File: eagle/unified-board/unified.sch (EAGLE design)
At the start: 96 parts, among them IC101 THAT151x, J1 eqout, J101 phantom, J103 eqout, J601 out2, U101 lme49710, U601 LM3915N, U602 lme49710

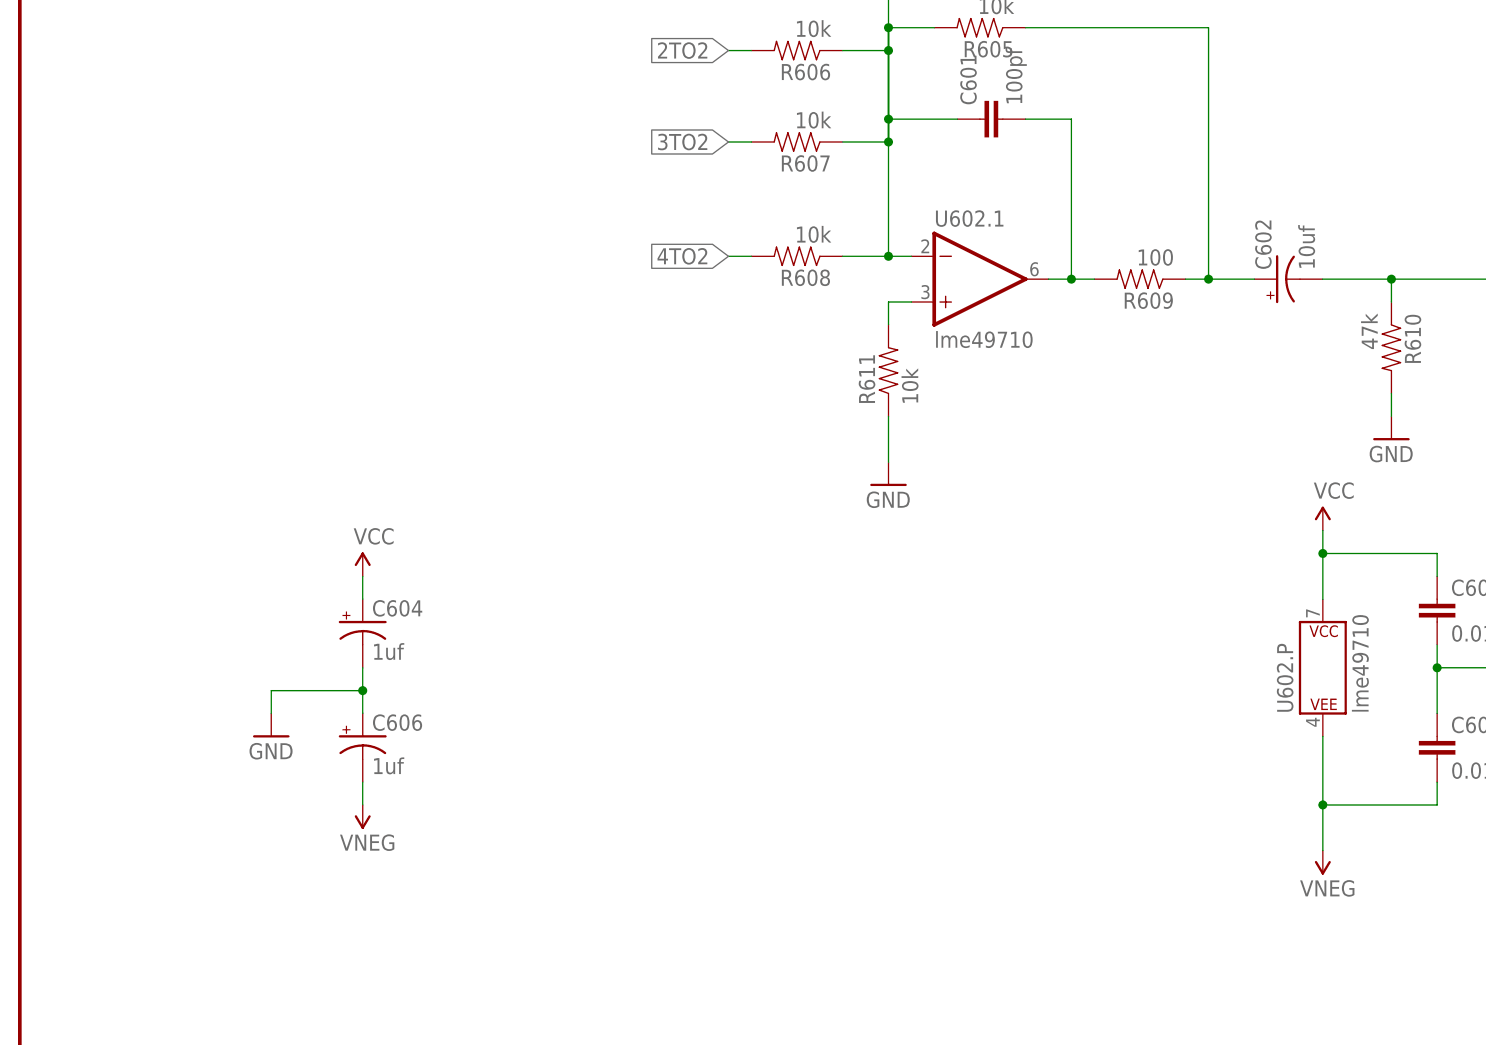
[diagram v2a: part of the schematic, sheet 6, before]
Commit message: Capacitor update
sourced & created a bunch of caps.
pushed components around more & better.
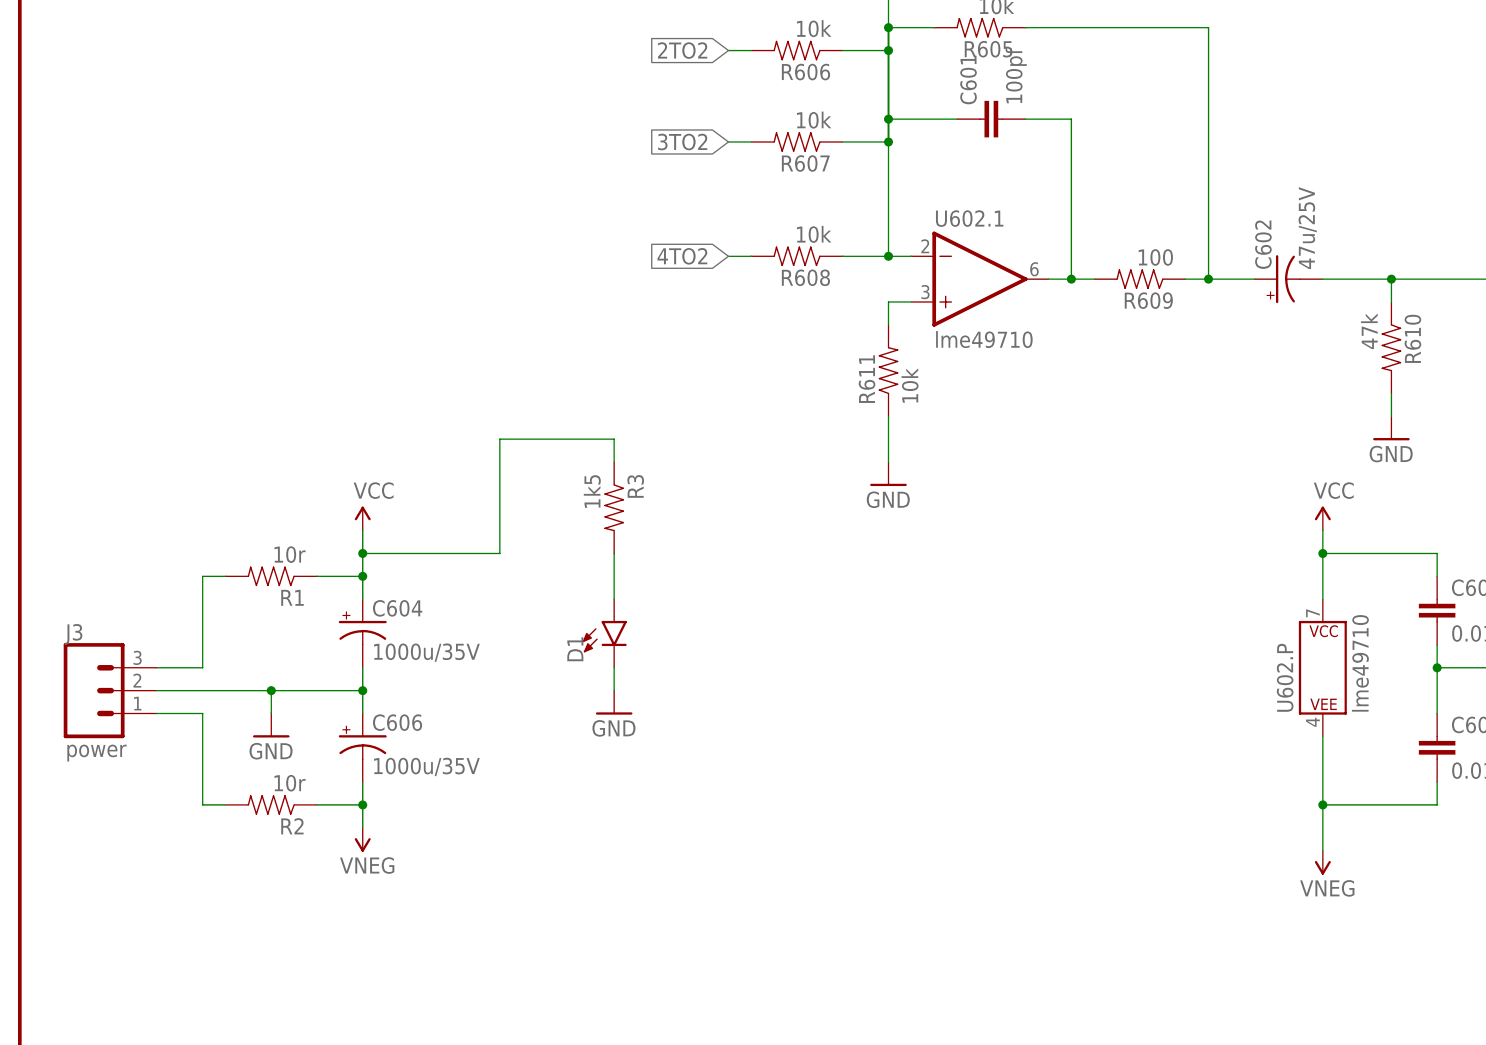
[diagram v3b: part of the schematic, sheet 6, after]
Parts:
- added D1: (no value), SparkFun-LED:LED5MM
- added J3: power, SparkFun-Connectors:CONN_03POLAR_LOCK
- added R1, R2: 10r, SparkFun-Resistors:RESISTORAXIAL-0.3
- added R3: 1k5, SparkFun-Resistors:RESISTORAXIAL-0.3
- C105, C114: value 22u -> 47u/63V; device SparkFun-Capacitors:100UF-25V-20%(PTH) -> mixer:CAP-LYTIC47U/63V
- C106, C107, C112, C116, C119, C121: value 470p -> 470pf; device SparkFun-Capacitors:CAPPTH -> mixer:CAP-CERAMIC470PF
- C108, C120: value 47p -> 47pf; device SparkFun-Capacitors:CAPPTH -> mixer:CAP-CERAMIC47PF
- C109, C117, C118, C122: value 22u -> 47u/25V; device SparkFun-Capacitors:100UF-25V-20%(PTH) -> mixer:CAP-LYTIC47U/25V
- C110, C601: device SparkFun-Capacitors:CAPPTH -> mixer:CAP-CERAMIC100PF
- C115: value 22u -> 6800u/25V; device SparkFun-Capacitors:100UF-25V-20%(PTH) -> mixer:CAP-LYTIC6800U/10V
- C602: value 10uf -> 47u/25V; device SparkFun-Capacitors:10UF-25V-20%(PTH) -> mixer:CAP-LYTIC47U/25V
- C604, C606: value 1uf -> 1000u/35V; device SparkFun-Capacitors:CAP_POLPTH2 -> mixer:CAP-LYTIC1000U/35V
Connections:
- new net N$18: J3.3, R1.2
- new net N$5: J3.1, R2.2
- new net N$54: D1.A, R3.2
- net GND: now also D1.C, J3.2, VR104.A, VR105.A
- net VCC: now also R1.1, R3.1
- net VNEG: now also R2.1
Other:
- note added: "Check DC offset at various EQ settings, possibly can omit C118"
- note added: "Check DC offset at various gains, possibly can omit C109"

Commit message: Conforming parts on BOM for ordering.
verified mouser & SFe part #s.
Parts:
- C603: device SparkFun-Capacitors:CAPPTH -> mixer:CAP-CERAMIC100PF
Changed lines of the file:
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@@
 <setting verticaltext="up"/>
 </settings>
-<grid distance="0.1" unitdist="inch" unit="inch" style="lines" multiple="1" display="yes" altdistance="0.01" altunitdist="inch" altunit="inch"/>
+<grid distance="0.1" unitdist="inch" unit="inch" style="lines" multiple="1" display="no" altdistance="0.01" altunitdist="inch" altunit="inch"/>
 <layers>
 <layer number="1" name="Top" color="4" fill="1" visible="no" active="no"/>
@@
 <part name="SUPPLY606" library="SparkFun-Aesthetics" deviceset="VCC" device=""/>
 <part name="FB601" library="mixer" deviceset="FB" device="" value="FB"/>
-<part name="C603" library="SparkFun-Capacitors" deviceset="CAP" device="PTH" value="100pf"/>
+<part name="C603" library="mixer" deviceset="CAP-CERAMIC" device="100PF" value="100pf"/>
 <part name="GND605" library="SparkFun-Aesthetics" deviceset="GND" device=""/>
 <part name="D602" library="mixer" deviceset="RECTIFIER" device="RB15X"/>

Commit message: Duplicated input channels.
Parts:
- removed D1: (no value), SparkFun-LED:LED5MM
- removed J1: eqout, SparkFun-Connectors:M01NOSILK-KIT
- removed J3: power, SparkFun-Connectors:CONN_03POLAR_LOCK
- removed R1, R2: 10r, SparkFun-Resistors:RESISTORAXIAL-0.3
- removed R3: 1k5, SparkFun-Resistors:RESISTORAXIAL-0.3
- added C201, C202, C301, C302, C401, C402: 47pf, mixer:CAP-CERAMIC47PF
- added C203, C204, C205, C206, C212, C213, C303, C304, C305, C306, C312, C313, C403, C404, C405, C406, C412, C413: 470pf, mixer:CAP-CERAMIC470PF
- added C207, C208, C307, C308, C407, C408: 47u/63V, mixer:CAP-LYTIC47U/63V
- added C209, C210, C214, C220, C309, C310, C314, C320, C409, C410, C414, C420: 47u/25V, mixer:CAP-LYTIC47U/25V
- added C211, C311, C411: 6800u/25V, mixer:CAP-LYTIC6800U/10V
- added C215, C216, C315, C316, C415, C416: 0.1uf, mixer:WIMA-MKS20.1UF
- added C217, C218, C317, C318, C417, C418: 0.015uf, mixer:WIMA-MKS20.015UF
- added C219, C319, C419: 100pf, mixer:CAP-CERAMIC100PF
- added C221, C222, C321, C322, C421, C422: 0.01uf, mixer:WIMA-MKS20.01UF
- added D201, D301, D401: RECTIFIERRB15X, mixer:RECTIFIERRB15X
- added D202, D203, D302, D303, D402, D403: 1N4148, SparkFun-DiscreteSemi:DIODE1N4148
- added D603: RED, SparkFun-LED:LED_BARGRAPH_10RED
- added IC201, IC301, IC401: THAT151x, mosfet:THAT151X
- added J105, J204, J205, J304, J305, J404, J405: eqout, SparkFun-Connectors:M01NOSILK-KIT
- added J201, J202, J301, J302, J401, J402: (no value), SparkFun-Connectors:M031X03_NO_SILK
- added J203, J303, J403: phantom, SparkFun-Connectors:M01NOSILK-KIT
- added J206, J306, J406: (no value), SparkFun-Connectors:CONN_05PTH_LONGPADS
- added J602: out2, SparkFun-Connectors:CONN_02LOCK_LONGPADS
- added R201, R202, R301, R302, R401, R402: 6k8, SparkFun-Resistors:10KOHM-1/4W-1%(PTH)HORIZ
- added R203, R204, R303, R304, R403, R404: 10, SparkFun-Resistors:10KOHM-1/4W-1%(PTH)HORIZ
- added R205, R206, R305, R306, R405, R406: 4k99, SparkFun-Resistors:10KOHM-1/4W-1%(PTH)HORIZ
- added R207, R307, R407: 22k, SparkFun-Resistors:10KOHM-1/4W-1%(PTH)HORIZ
- added R208, R209, R308, R309, R408, R409: 1k2, SparkFun-Resistors:10KOHM-1/4W-1%(PTH)HORIZ
- added R210, R310, R410: 5, SparkFun-Resistors:10KOHM-1/4W-1%(PTH)HORIZ
- added R211, R212, R311, R312, R411, R412: 1k8, SparkFun-Resistors:10KOHM-1/4W-1%(PTH)HORIZ
- added R213, R313, R413: 12k, SparkFun-Resistors:10KOHM-1/4W-1%(PTH)HORIZ
- added R214, R215, R216, R314, R315, R316, R414, R415, R416: 1k, SparkFun-Resistors:10KOHM-1/4W-1%(PTH)HORIZ
- added R612, R613, R614: ???, SparkFun-Resistors:RESISTORAXIAL-0.3
- added U201, U301, U401: lme49710, mixer:OPAMPLME49710
- added VR201, VR301, VR401: 10K, mixer:POTROT-SW-POT
- added VR202, VR203, VR204, VR205, VR302, VR303, VR304, VR305, VR402, VR403, VR404, VR405: 10K, mixer:POT10K-VERTPIN
- C101, C102: value 0.01uf -> 47pf; device mixer:WIMA-MKS20.01UF -> mixer:CAP-CERAMIC47PF
- C103: value 0.015uf -> 470pf; device mixer:WIMA-MKS20.015UF -> mixer:CAP-CERAMIC470PF
- C104, C113: value 0.1uf -> 470pf; device mixer:WIMA-MKS20.1UF -> mixer:CAP-CERAMIC470PF
- C105: value 47u/63V -> 470pf; device mixer:CAP-LYTIC47U/63V -> mixer:CAP-CERAMIC470PF
- C107: value 470pf -> 47u/63V; device mixer:CAP-CERAMIC470PF -> mixer:CAP-LYTIC47U/63V
- C108: value 47pf -> 47u/63V; device mixer:CAP-CERAMIC47PF -> mixer:CAP-LYTIC47U/63V
- C110: value 100pf -> 47u/25V; device mixer:CAP-CERAMIC100PF -> mixer:CAP-LYTIC47U/25V
- C111: value 0.015uf -> 6800u/25V; device mixer:WIMA-MKS20.015UF -> mixer:CAP-LYTIC6800U/10V
- C114: value 47u/63V -> 47u/25V; device mixer:CAP-LYTIC47U/63V -> mixer:CAP-LYTIC47U/25V
- C115: value 6800u/25V -> 0.1uf; device mixer:CAP-LYTIC6800U/10V -> mixer:WIMA-MKS20.1UF
- C116: value 470pf -> 0.1uf; device mixer:CAP-CERAMIC470PF -> mixer:WIMA-MKS20.1UF
- C117, C118: value 47u/25V -> 0.015uf; device mixer:CAP-LYTIC47U/25V -> mixer:WIMA-MKS20.015UF
- C119: value 470pf -> 100pf; device mixer:CAP-CERAMIC470PF -> mixer:CAP-CERAMIC100PF
- C120: value 47pf -> 47u/25V; device mixer:CAP-CERAMIC47PF -> mixer:CAP-LYTIC47U/25V
- C121: value 470pf -> 0.01uf; device mixer:CAP-CERAMIC470PF -> mixer:WIMA-MKS20.01UF
- C122: value 47u/25V -> 0.01uf; device mixer:CAP-LYTIC47U/25V -> mixer:WIMA-MKS20.01UF
- C601: value 100pf -> 1000u/35V; device mixer:CAP-CERAMIC100PF -> mixer:CAP-LYTIC1000U/35V
- C602: value 47u/25V -> 1000u/35V; device mixer:CAP-LYTIC47U/25V -> mixer:CAP-LYTIC1000U/35V
- C604: value 1000u/35V -> 47u/25V; device mixer:CAP-LYTIC1000U/35V -> mixer:CAP-LYTIC47U/25V
- C606: value 1000u/35V -> 0.01uf; device mixer:CAP-LYTIC1000U/35V -> mixer:WIMA-MKS20.01UF
- C607: value 0.01uf -> 100pf; device mixer:WIMA-MKS20.01UF -> mixer:CAP-CERAMIC100PF
- D601: value RED -> (none); device SparkFun-LED:LED_BARGRAPH_10RED -> SparkFun-LED:LED5MM
- J101: value phantom -> (none); device SparkFun-Connectors:M01NOSILK-KIT -> SparkFun-Connectors:M031X03_NO_SILK
- J103: value eqout -> phantom
- J104: value (none) -> eqout; device SparkFun-Connectors:M031X03_NO_SILK -> SparkFun-Connectors:M01NOSILK-KIT
- J601: value out2 -> power; device SparkFun-Connectors:CONN_02LOCK_LONGPADS -> SparkFun-Connectors:CONN_03POLAR_LOCK
- R101: value 1k8 -> 6k8
- R102: value 1k -> 6k8
- R103: value 6k8 -> 10
- R105: value 1k -> 4k99
- R106: value 1k2 -> 4k99
- R107: value 12k -> 22k
- R108: value 6k8 -> 1k2
- R111: value 10 -> 1k8
- R113: value 1k -> 12k
- R114: value 22k -> 1k
- R115, R116: value 4k99 -> 1k
- R601, R602: value ??? -> 10r
- R603: value ??? -> 1k5
- R609: value 100 -> 10k
- R610: value 47k -> 100
- R611: value 10k -> 47k
- U601: value LM3915N -> lme49710; device SparkFun-IC-Special-Function:LM3915N -> mixer:OPAMPLME49710
- U602: value lme49710 -> LM3915N; device mixer:OPAMPLME49710 -> SparkFun-IC-Special-Function:LM3915N
- VR101: device mixer:POT10K-VERTPIN -> mixer:POTROT-SW-POT
- VR103: device mixer:POTROT-SW-POT -> mixer:POT10K-VERTPIN
- renumbered H1 to H612, H10 to H603, H11 to H601, H12 to H602, H2 to H611, H3 to H609, H4 to H610, H5 to H608, H6 to H607, H7 to H605, H8 to H606, H9 to H604, J2 to J106
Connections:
- new net EQ1OUT1: C220.-, J205.1, J206.1
- new net EQ1OUT2: C320.-, J305.1, J306.1
- new net EQ1OUT3: C420.-, J405.1, J406.1
- new net HIGHEST: D603.C, U602.LED10
- new net LOWEST: D603.C9, U602.LED1
- new net N$100: C307.-, R303.2
- new net N$101: R307.1, R308.2, R309.1
- new net N$102: C311.-, D303.A, IC301.RG2
- new net N$103: D302.A, IC301.RG1, VR301.A, VR301.S
- new net N$104: C318.1, VR303.E
- new net N$105: C317.2, VR303.A
- new net N$106: R310.1, VR301.E
- new net N$107: C311.+, R310.2
- new net N$108: C302.1, J302.2
- new net N$109: C302.2, C305.2, C306.1
- new net N$110: C305.1, C309.+, J302.3
- new net N$111: C306.2, C310.+, J302.1
- new net N$112: C310.-, R306.2
- new net N$113: C309.-, R305.2
- new net N$114: D301.~, D302.C, IC301.-IN, R303.1, R305.1, R308.1
- new net N$115: D301.~2, D303.C, IC301.+IN, R304.1, R306.1, R309.2
- new net N$116: C319.2, C320.+, R311.2, R315.2, U301.1.OUT
- new net N$117: C414.-, J404.1, R412.1, R416.1
- new net N$118: C415.1, R411.1, VR402.A
- new net N$119: C416.1, R412.2, VR402.E
- new net N$120: R414.1, VR403.S
- new net N$121: C415.2, C416.2, R413.2, VR402.S
- new net N$122: C418.2, R416.2
- new net N$123: C417.1, R415.1
- new net N$124: C419.1, R413.1, R414.2, U401.1.-IN
- new net N$125: C414.+, IC401.OUT
- new net N$126: C401.1, J401.2
- new net N$127: C401.2, C403.2, C404.1
- new net N$128: C403.1, C407.+, J401.3, R401.1
- new net N$129: C404.2, C408.+, J401.1, R402.1
- new net N$130: C408.-, R404.2
- new net N$131: J403.1, R401.2, R402.2
- new net N$132: C407.-, R403.2
- new net N$133: R407.1, R408.2, R409.1
- new net N$134: C411.-, D403.A, IC401.RG2
- new net N$135: D402.A, IC401.RG1, VR401.A, VR401.S
- new net N$136: C418.1, VR403.E
- new net N$137: C417.2, VR403.A
- new net N$138: R410.1, VR401.E
- new net N$139: C411.+, R410.2
- new net N$140: C402.1, J402.2
- new net N$141: C402.2, C405.2, C406.1
- new net N$142: C405.1, C409.+, J402.3
- new net N$143: C406.2, C410.+, J402.1
- new net N$144: C410.-, R406.2
- new net N$145: C409.-, R405.2
- new net N$146: D401.~, D402.C, IC401.-IN, R403.1, R405.1, R408.1
- new net N$147: D401.~2, D403.C, IC401.+IN, R404.1, R406.1, R409.2
- new net N$148: C419.2, C420.+, R411.2, R415.2, U401.1.OUT
- new net N$55: C216.1, R212.2, VR202.E
- new net N$56: R214.1, VR203.S
- new net N$57: C215.2, C216.2, R213.2, VR202.S
- new net N$58: C218.2, R216.2
- new net N$59: C217.1, R215.1
- new net N$60: C219.1, R213.1, R214.2, U201.1.-IN
- new net N$61: C214.+, IC201.OUT
- new net N$62: C201.1, J201.2
- new net N$63: C201.2, C203.2, C204.1
- new net N$64: C203.1, C207.+, J201.3, R201.1
- new net N$65: C204.2, C208.+, J201.1, R202.1
- new net N$66: C208.-, R204.2
- new net N$67: J203.1, R201.2, R202.2
- new net N$68: C207.-, R203.2
- new net N$69: R207.1, R208.2, R209.1
- new net N$70: C211.-, D203.A, IC201.RG2
- new net N$71: D202.A, IC201.RG1, VR201.A, VR201.S
- new net N$72: C218.1, VR203.E
- new net N$73: C217.2, VR203.A
- new net N$74: R210.1, VR201.E
- new net N$75: C211.+, R210.2
- new net N$76: C202.1, J202.2
- new net N$77: C202.2, C205.2, C206.1
- new net N$78: C205.1, C209.+, J202.3
- new net N$79: C206.2, C210.+, J202.1
- new net N$80: C210.-, R206.2
- new net N$81: C209.-, R205.2
- new net N$82: D201.~, D202.C, IC201.-IN, R203.1, R205.1, R208.1
- new net N$83: D201.~2, D203.C, IC201.+IN, R204.1, R206.1, R209.2
- new net N$84: C219.2, C220.+, R211.2, R215.2, U201.1.OUT
- new net N$85: C314.-, J304.1, R312.1, R316.1
- new net N$86: C315.1, R311.1, VR302.A
- new net N$87: C316.1, R312.2, VR302.E
- new net N$88: R314.1, VR303.S
- new net N$89: C315.2, C316.2, R313.2, VR302.S
- new net N$90: C318.2, R316.2
- new net N$91: C317.1, R315.1
- new net N$92: C319.1, R313.1, R314.2, U301.1.-IN
- new net N$93: C314.+, IC301.OUT
- new net N$94: C301.1, J301.2
- new net N$95: C301.2, C303.2, C304.1
- new net N$96: C303.1, C307.+, J301.3, R301.1
- new net N$97: C304.2, C308.+, J301.1, R302.1
- new net N$98: C308.-, R304.2
- new net N$99: J303.1, R301.2, R302.2
- net 1TO1: now also J206.2, J306.2, J406.2
- net 1TO2: now also J206.3, J306.3, J406.3
- net 2TO2: now also R605.2; no longer R606.2
- net 3TO2: now also R606.2; no longer R607.2
- net 4TO2: now also R607.2; no longer R608.2
- net EQ1OUT: now also C120.-, J105.1; no longer C118.-, J103.1
- net GND: now also C112.2, C113.2, C121.2, C122.1, C212.2, C213.2, C221.2, C222.1, C312.2, C313.2, C321.2, C322.1, C412.2, C413.2, C421.2, C422.1, C601.-, C602.+, C606.1, C607.2, D601.C, IC201.REF, IC301.REF, IC401.REF, J206.4, J206.5, J306.4, J306.5, J406.4, J406.5, J602.2, R107.2, R207.2, R307.2, R407.2, R608.1, R611.2, R612.2, U201.1.+IN, U301.1.+IN, U401.1.+IN, U602.RLO, U602.V-, VR204.A, VR205.A, VR304.A, VR305.A, VR404.A, VR405.A; no longer C101.2, C102.1, C106.2, C116.2, C603.2, C604.-, C606.+, C607.1, D1.C, J3.2, R114.2, R602.2, R610.2, R611.1, U601.RLO, U601.V-
- net N$1: now also C115.1, R111.1; no longer C104.1, R101.1
- net N$10: now also C118.1, VR103.E; no longer C111.1, VR101.E
- net N$11: now also C604.-, R611.1, U602.SIGIN; no longer C602.-, R610.1, U601.SIGIN
- net N$12: now also C604.+, R610.1; no longer C602.+, R605.1
- net N$13: now also R608.2, U601.1.+IN; no longer R611.2, U602.1.+IN
- net N$14: now also C115.2, C116.2, R113.2; no longer C104.2, C113.2, R107.2
- net N$15: now also C117.2, VR103.A; no longer C103.2, VR101.A
- net N$16: now also C603.2, R610.2, U601.1.OUT; no longer C601.2, R609.2, U602.1.OUT
- net N$17: now also C603.1, R605.1, R609.2, U601.1.-IN; no longer C601.1, R605.2, R608.1, U602.1.-IN
- net N$18: now also J601.3, R601.2; no longer J3.3, R1.2
- net N$19: now also C117.1, R115.1; no longer C103.1, R102.1
- net N$2: now also C116.1; no longer C113.1
- net N$20: now also C214.-, J204.1, R212.1, R216.1; no longer D601.C9, U601.LED1
- net N$21: now also C111.-; no longer C115.-
- net N$22: now also C114.+; no longer C109.+
- net N$23: now also C101.1, J101.2; no longer C108.1, J102.2
- net N$24: now also C101.2, C103.2, C104.1; no longer C107.2, C108.2, C112.1
- net N$25: now also C103.1, C107.+, J101.3, R101.1; no longer C105.+, C107.1, J102.3, R103.1
- net N$26: now also C104.2, C108.+, J101.1, R102.1; no longer C112.2, C114.+, J102.1, R108.1
- net N$27: now also C108.-, R104.2; no longer C114.-, R111.2
- net N$28: now also J103.1, R101.2, R102.2; no longer J101.1, R103.2, R108.2
- net N$29: now also C107.-, R103.2; no longer C105.-, R104.2
- net N$3: now also C119.1, R113.1, R114.2; no longer C110.1, R105.2, R107.1
- net N$30: now also R103.1, R105.1, R108.1; no longer R104.1, R106.1, R115.1
- net N$31: now also R104.1, R106.1; no longer R111.1, R116.1
- net N$32: now also R107.1, R108.2; no longer R106.2, R114.1
- net N$33: now also VR101.A, VR101.S; no longer VR103.A, VR103.S
- net N$34: now also VR101.E; no longer VR103.E
- net N$35: now also C111.+; no longer C115.+
- net N$36: now also C102.1, J102.2; no longer C120.1, J104.2
- net N$37: now also C102.2, C105.2, C106.1; no longer C119.2, C120.2, C121.1
- net N$38: now also C105.1, C109.+, J102.3; no longer C117.+, C119.1, J104.3
- net N$39: now also C106.2, C110.+, J102.1; no longer C121.2, C122.+, J104.1
- net N$4: now also C118.2, R116.2; no longer C111.2, R113.2
- net N$40: now also C110.-, R106.2; no longer C122.-, R116.2
- net N$41: now also D603.C8, U602.LED2; no longer D601.C8, U601.LED2
- net N$42: now also C109.-, R105.2; no longer C117.-, R115.2
- net N$43: now also D603.C7, U602.LED3; no longer D601.C7, U601.LED3
- net N$44: now also D603.C6, U602.LED4; no longer D601.C6, U601.LED4
- net N$45: now also D603.C5, U602.LED5; no longer D601.C5, U601.LED5
- net N$46: now also D603.C4, U602.LED6; no longer D601.C4, U601.LED6
- net N$47: now also D603.C3, U602.LED7; no longer D601.C3, U601.LED7
- net N$48: now also D603.C2, U602.LED8; no longer D601.C2, U601.LED8
- net N$49: now also D603.C1, U602.LED9; no longer D601.C1, U601.LED9
- net N$5: now also J601.1, R602.2; no longer J3.1, R2.2
- net N$50: now also C215.1, R211.1, VR202.A; no longer D601.C, U601.LED10
- net N$51: now also R613.1, R614.2, U602.REFOUT; no longer R601.2, R603.1, U601.REFOUT
- net N$52: now also R612.1, R613.2, U602.REFADJ; no longer R602.1, R603.2, U601.REFADJ
- net N$53: now also R614.1, U602.RHI; no longer R601.1, U601.RHI
- net N$54: now also D601.A, R603.2; no longer D1.A, R3.2
- net N$6: now also C119.2, C120.+, R111.2, R115.2; no longer C110.2, C118.+, R101.2, R102.2
- net N$7: now also C607.1, J602.1; no longer C603.1, J601.1
- net N$8: now also R114.1, VR103.S; no longer R105.1, VR101.S
- net N$9: now also C114.-, J104.1, R116.1; no longer C109.-, J1.1, R113.1
- net VCC: now also C112.1, C121.1, C212.1, C221.1, C312.1, C321.1, C412.1, C421.1, C601.+, D201.+, D301.+, D401.+, D603.A, D603.A1, D603.A2, D603.A3, D603.A4, D603.A5, D603.A6, D603.A7, D603.A8, D603.A9, IC201.V+, IC301.V+, IC401.V+, R601.1, R603.1, U201.P.P$V+, U301.P.P$V+, U401.P.P$V+, U601.P.P$V+, U602.V+; no longer C101.1, C106.1, C604.+, D601.A, D601.A1, D601.A2, D601.A3, D601.A4, D601.A5, D601.A6, D601.A7, D601.A8, D601.A9, R1.1, R3.1, U601.V+, U602.P.P$V+
- net VNEG: now also C113.1, C122.2, C213.1, C222.2, C313.1, C322.2, C413.1, C422.2, C602.-, C606.2, D201.-, D301.-, D401.-, IC201.V-, IC301.V-, IC401.V-, R602.1, U201.P.P$V-, U301.P.P$V-, U401.P.P$V-, U601.P.P$V-; no longer C102.2, C116.1, C606.-, C607.2, R2.1, U602.P.P$V-
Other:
- moved on the sheet: C101, C102, C103, C104, C106, C109, C112, C113, C114, C116, C119, C121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

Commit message: Assigning net classes, second summing channel.
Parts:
- removed C606: 0.01uf, mixer:WIMA-MKS20.01UF
- removed C607: 100pf, mixer:CAP-CERAMIC100PF
- removed D603: RED, SparkFun-LED:LED_BARGRAPH_10RED
- removed J602: out2, SparkFun-Connectors:CONN_02LOCK_LONGPADS
- removed R612, R613, R614: ???, SparkFun-Resistors:RESISTORAXIAL-0.3
- added C501, C505: 100pf, mixer:CAP-CERAMIC100PF
- added C502: 47u/25V, mixer:CAP-LYTIC47U/25V
- added C503, C504: 0.01uf, mixer:WIMA-MKS20.01UF
- added C701, C702: 1000u/35V, mixer:CAP-LYTIC1000U/35V
- added D501: RECTIFIERRB15X, mixer:RECTIFIERRB15X
- added D502: RED, SparkFun-LED:LED_BARGRAPH_10RED
- added D701: (no value), SparkFun-LED:LED5MM
- added FB501: FB, mixer:FB
- added FRAME701: FRAME-LEDGER, SparkFun-Aesthetics:FRAME-LEDGER
- added J501: out2, SparkFun-Connectors:CONN_02LOCK_LONGPADS
- added J701: power, SparkFun-Connectors:CONN_03POLAR_LOCK
- added R501, R502, R503, R504, R505, R506: 10k, SparkFun-Resistors:RESISTORAXIAL-0.3
- added R507: 100, SparkFun-Resistors:RESISTORAXIAL-0.3
- added R508: 47k, SparkFun-Resistors:RESISTORAXIAL-0.3
- added R509, R510, R511: ???, SparkFun-Resistors:RESISTORAXIAL-0.3
- added R701, R702: 10r, SparkFun-Resistors:RESISTORAXIAL-0.3
- added R703: 1k5, SparkFun-Resistors:RESISTORAXIAL-0.3
- added U501: lme49710, mixer:OPAMPLME49710
- added U502: LM3915N, SparkFun-IC-Special-Function:LM3915N
- C601: value 1000u/35V -> 100pf; device mixer:CAP-LYTIC1000U/35V -> mixer:CAP-CERAMIC100PF
- C602: value 1000u/35V -> 47u/25V; device mixer:CAP-LYTIC1000U/35V -> mixer:CAP-LYTIC47U/25V
- C603: value 100pf -> 0.01uf; device mixer:CAP-CERAMIC100PF -> mixer:WIMA-MKS20.01UF
- C604: value 47u/25V -> 0.01uf; device mixer:CAP-LYTIC47U/25V -> mixer:WIMA-MKS20.01UF
- C605: value 0.01uf -> 100pf; device mixer:WIMA-MKS20.01UF -> mixer:CAP-CERAMIC100PF
- D601: value (none) -> RECTIFIERRB15X; device SparkFun-LED:LED5MM -> mixer:RECTIFIERRB15X
- D602: value RECTIFIERRB15X -> RED; device mixer:RECTIFIERRB15X -> SparkFun-LED:LED_BARGRAPH_10RED
- J601: value power -> out2; device SparkFun-Connectors:CONN_03POLAR_LOCK -> SparkFun-Connectors:CONN_02LOCK_LONGPADS
- R601, R602: value 10r -> 10k
- R603: value 1k5 -> 10k
- R607: value 10k -> 100
- R608: value 10k -> 47k
- R609: value 10k -> ???
- R610: value 100 -> ???
- R611: value 47k -> ???
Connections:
- removed net N$18: J601.3, R601.2
- removed net N$5: J601.1, R602.2
- removed net N$54: D601.A, R603.2
- new net 2TO1: J206.2, R502.2
- new net 3TO1: J306.2, R503.2
- new net 4TO1: J406.2, R504.2
- new net HIGHEST1: D502.C, U502.LED10
- new net LOWEST1: D502.C9, U502.LED1
- new net N$149: R505.2, U501.1.+IN
- new net N$150: C501.1, R501.1, R502.1, R503.1, R504.1, R506.2, U501.1.-IN
- new net N$151: C505.1, FB501.2, J501.1
- new net N$152: C502.-, D501.~, D501.~2, FB501.1, R508.1, U502.SIGIN
- new net N$153: D502.C8, U502.LED2
- new net N$154: D502.C7, U502.LED3
- new net N$155: D502.C6, U502.LED4
- new net N$156: D502.C5, U502.LED5
- new net N$157: D502.C4, U502.LED6
- new net N$158: D502.C3, U502.LED7
- new net N$159: D502.C2, U502.LED8
- new net N$160: D502.C1, U502.LED9
- new net N$161: R510.1, R511.2, U502.REFOUT
- new net N$162: R509.1, R510.2, U502.REFADJ
- new net N$163: C501.2, R507.2, U501.1.OUT
- new net N$164: C502.+, R506.1, R507.1
- new net N$165: R511.1, U502.RHI
- new net N$166: J701.1, R702.2
- new net N$167: J701.3, R701.2
- new net N$168: D701.A, R703.2
- net 1TO1: now also R501.2; no longer J206.2, J306.2, J406.2
- net 1TO2: now also R601.2; no longer J206.3, J306.3, J406.3, R604.2
- net 2TO2: now also J206.3, R602.2; no longer R605.2
- net 3TO2: now also J306.3, R603.2; no longer R606.2
- net 4TO2: now also J406.3, R604.2; no longer R607.2
- net GND: now also C503.2, C504.1, C505.2, C603.2, C604.1, C701.-, C702.+, D701.C, J501.2, J701.2, R505.1, R508.2, R509.2, R605.1, R608.2, R609.2, U502.RLO, U502.V-; no longer C601.-, C602.+, C606.1, C607.2, D601.C, J602.2, R608.1, R611.2, R612.2
- net HIGHEST: now also D602.C; no longer D603.C
- net LOWEST: now also D602.C9; no longer D603.C9
- net N$11: now also C602.-, D601.~, D601.~2, R608.1; no longer C604.-, D602.~, D602.~2, R611.1
- net N$12: now also C602.+, R606.1, R607.1; no longer C604.+, R609.1, R610.1
- net N$13: now also R605.2; no longer R608.2
- net N$16: now also C601.2, R607.2; no longer C603.2, R610.2
- net N$17: now also C601.1, R601.1, R602.1, R603.1, R606.2; no longer C603.1, R605.1, R606.1, R607.1, R609.2
- net N$41: now also D602.C8; no longer D603.C8
- net N$43: now also D602.C7; no longer D603.C7
- net N$44: now also D602.C6; no longer D603.C6
- net N$45: now also D602.C5; no longer D603.C5
- net N$46: now also D602.C4; no longer D603.C4
- net N$47: now also D602.C3; no longer D603.C3
- net N$48: now also D602.C2; no longer D603.C2
- net N$49: now also D602.C1; no longer D603.C1
- net N$51: now also R610.1, R611.2; no longer R613.1, R614.2
- net N$52: now also R609.1, R610.2; no longer R612.1, R613.2
- net N$53: now also R611.1; no longer R614.1
- net N$7: now also C605.1, J601.1; no longer C607.1, J602.1
- net VCC: now also C503.1, C603.1, C701.+, D501.+, D502.A, D502.A1, D502.A2, D502.A3, D502.A4, D502.A5, D502.A6, D502.A7, D502.A8, D502.A9, D601.+, D602.A, D602.A1, D602.A2, D602.A3, D602.A4, D602.A5, D602.A6, D602.A7, D602.A8, D602.A9, R701.1, R703.1, U501.P.P$V+, U502.V+; no longer C601.+, C605.1, D602.+, D603.A, D603.A1, D603.A2, D603.A3, D603.A4, D603.A5, D603.A6, D603.A7, D603.A8, D603.A9, R601.1, R603.1
- net VNEG: now also C504.2, C604.2, C702.-, D501.-, D601.-, R702.1, U501.P.P$V-; no longer C602.-, C606.2, D602.-, R602.1
